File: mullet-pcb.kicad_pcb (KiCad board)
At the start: 2 copper layers, 299.7 x 97.7 mm, 187 parts, among them SW1 KEYSW, SW10 KEYSW, SW11 KEYSW, SW12 KEYSW, SW13 KEYSW, SW14 KEYSW, SW15 KEYSW, SW16 KEYSW, SW17 KEYSW, SW18 KEYSW, SW19 KEYSW, SW2 KEYSW, SW20 KEYSW, SW21 KEYSW, SW22 KEYSW, SW23 KEYSW, SW24 KEYSW, SW25 KEYSW, SW26 KEYSW, SW27 KEYSW, SW28 KEYSW, SW29 KEYSW, SW3 KEYSW, SW30 KEYSW, SW31 KEYSW, SW32 KEYSW, SW33 KEYSW, SW34 KEYSW, SW35 KEYSW, SW36 KEYSW, SW37 KEYSW, SW38 KEYSW, SW39 KEYSW, SW4 KEYSW, SW40 KEYSW, SW41 KEYSW, SW42 KEYSW, SW43 KEYSW, SW44 KEYSW, SW45 KEYSW, SW46 KEYSW, SW47 KEYSW, SW48 KEYSW, SW49 KEYSW, SW5 KEYSW, SW50 KEYSW, SW51 KEYSW, SW52 KEYSW, SW53 KEYSW, SW54 KEYSW, SW55 KEYSW, SW56 KEYSW, SW57 KEYSW, SW58 KEYSW, SW59 KEYSW, SW6 KEYSW, SW60 KEYSW, SW61 KEYSW, SW62 KEYSW, SW63 KEYSW, SW64 KEYSW, SW65 KEYSW, SW66 KEYSW, SW67 KEYSW, SW7 KEYSW, SW8 KEYSW, SW9 KEYSW, U1 ATMEGA32U4, U2 PRTR5V0U2X, X1 XTAL_GND

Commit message: Update gnd fills for xtal
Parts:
- R6: value 22 -> 22Ω
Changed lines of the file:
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@@
     (tags resistor)
     (attr smd)
-    (fp_text reference R1 (at 0.682409 -1.679776 180) (layer B.SilkS)
-      (effects (font (size 1 1) (thickness 0.15)) (justify mirror))
+    (fp_text reference R1 (at 0.577423 -1.679776 180) (layer B.SilkS)
+      (effects (font (size 0.8 0.8) (thickness 0.15)) (justify mirror))
     )
     (fp_text value 5.1k (at -0.787395 -1.994734 180) (layer B.SilkS)
@@
     (tags resistor)
     (attr smd)
-    (fp_text reference R2 (at 2.047227 -0.104986 180) (layer B.SilkS)
-      (effects (font (size 1 1) (thickness 0.15)) (justify mirror))
+    (fp_text reference R2 (at 2.414678 1.522297 180) (layer B.SilkS)
+      (effects (font (size 0.8 0.8) (thickness 0.15)) (justify mirror))
     )
-    (fp_text value 5.1k (at -2.09972 -0.052493 180) (layer B.SilkS)
+    (fp_text value 5.1k (at 1.364818 1.942241 180) (layer B.SilkS)
       (effects (font (size 0.8 0.8) (thickness 0.15)) (justify mirror))
     )
@@
     (tags resistor)
     (attr smd)
-    (fp_text reference F1 (at -2.467171 -0.157479 180) (layer B.SilkS)
+    (fp_text reference F1 (at -2.467171 -0.52493 180) (layer B.SilkS)
       (effects (font (size 1 1) (thickness 0.15)) (justify mirror))
     )
@@
     (tags resistor)
     (attr smd)
-    (fp_text reference R5 (at -2.309692 -0.157479 180) (layer B.SilkS)
+    (fp_text reference R5 (at -2.467171 -0.271933 180) (layer B.SilkS)
       (effects (font (size 1 1) (thickness 0.15)) (justify mirror))
     )
@@
     (tags resistor)
     (attr smd)
-    (fp_text reference R6 (at -2.309692 0.052493 180) (layer B.SilkS)
+    (fp_text reference R6 (at -2.467171 0.314958 180) (layer B.SilkS)
       (effects (font (size 1 1) (thickness 0.15)) (justify mirror))
     )
-    (fp_text value 22 (at -3.727003 0.997367 180) (layer B.SilkS)
+    (fp_text value 22Ω (at -3.831989 -0.839888 180) (layer B.SilkS)
       (effects (font (size 1 1) (thickness 0.15)) (justify mirror))
     )

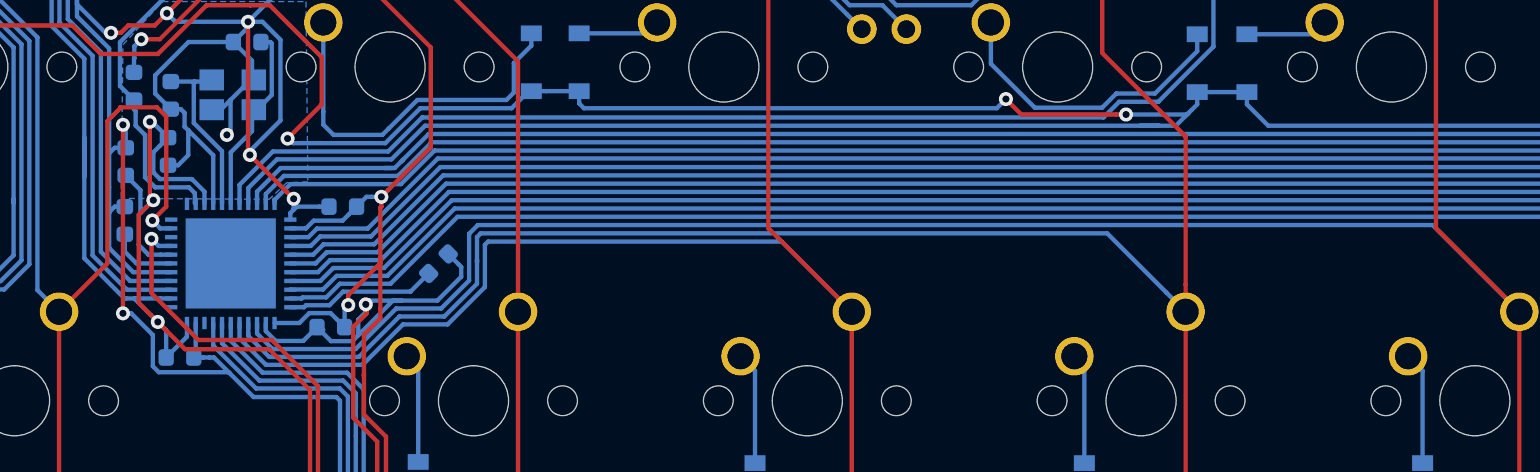
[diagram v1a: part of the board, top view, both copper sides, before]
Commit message: cleaned up traces
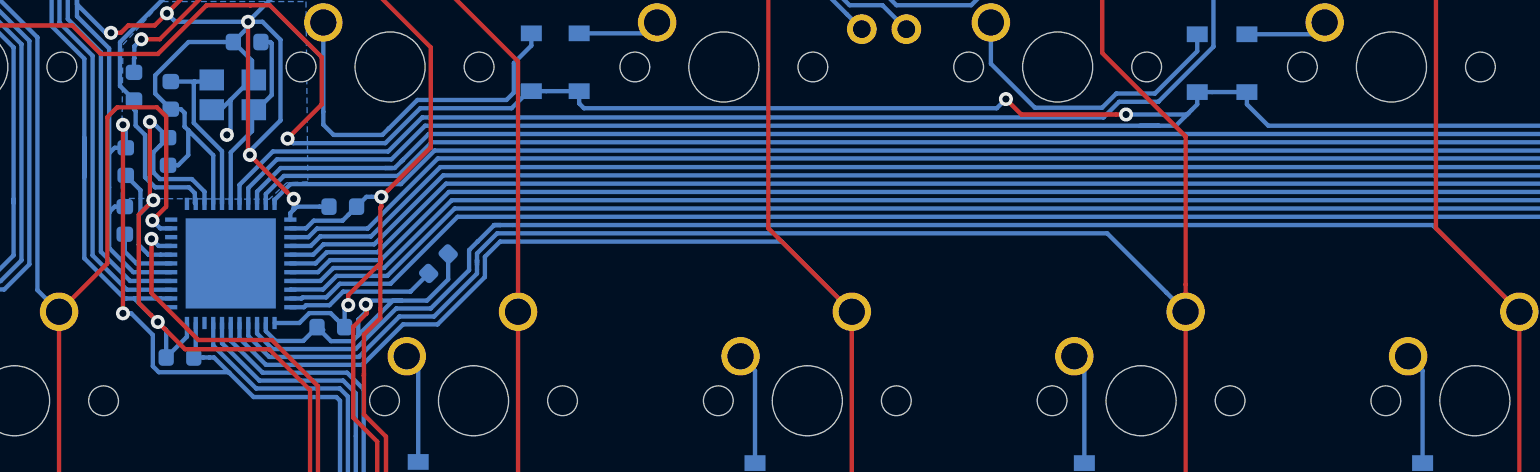
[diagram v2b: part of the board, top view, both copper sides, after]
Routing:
- net GND: track 1167.7 -> 1166.7 mm
- net col2: track 141.4 -> 140.7 mm
- net col3: track 143.1 -> 142.5 mm
- net col4: track 179.8 -> 179.3 mm
